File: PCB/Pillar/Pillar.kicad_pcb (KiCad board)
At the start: 2 copper layers, 100 x 86.6 mm, 39 parts, among them CN1 GROVE, CN2 GROVE, CN3 GROVE, CN4 GROVE, CN5 GROVE, CN6 TTL-232R-3V3, CN7 ST-LINK, CN8 Conn_01x05_Female, CN9 CardEdgeConnector5P, SW1 RESET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

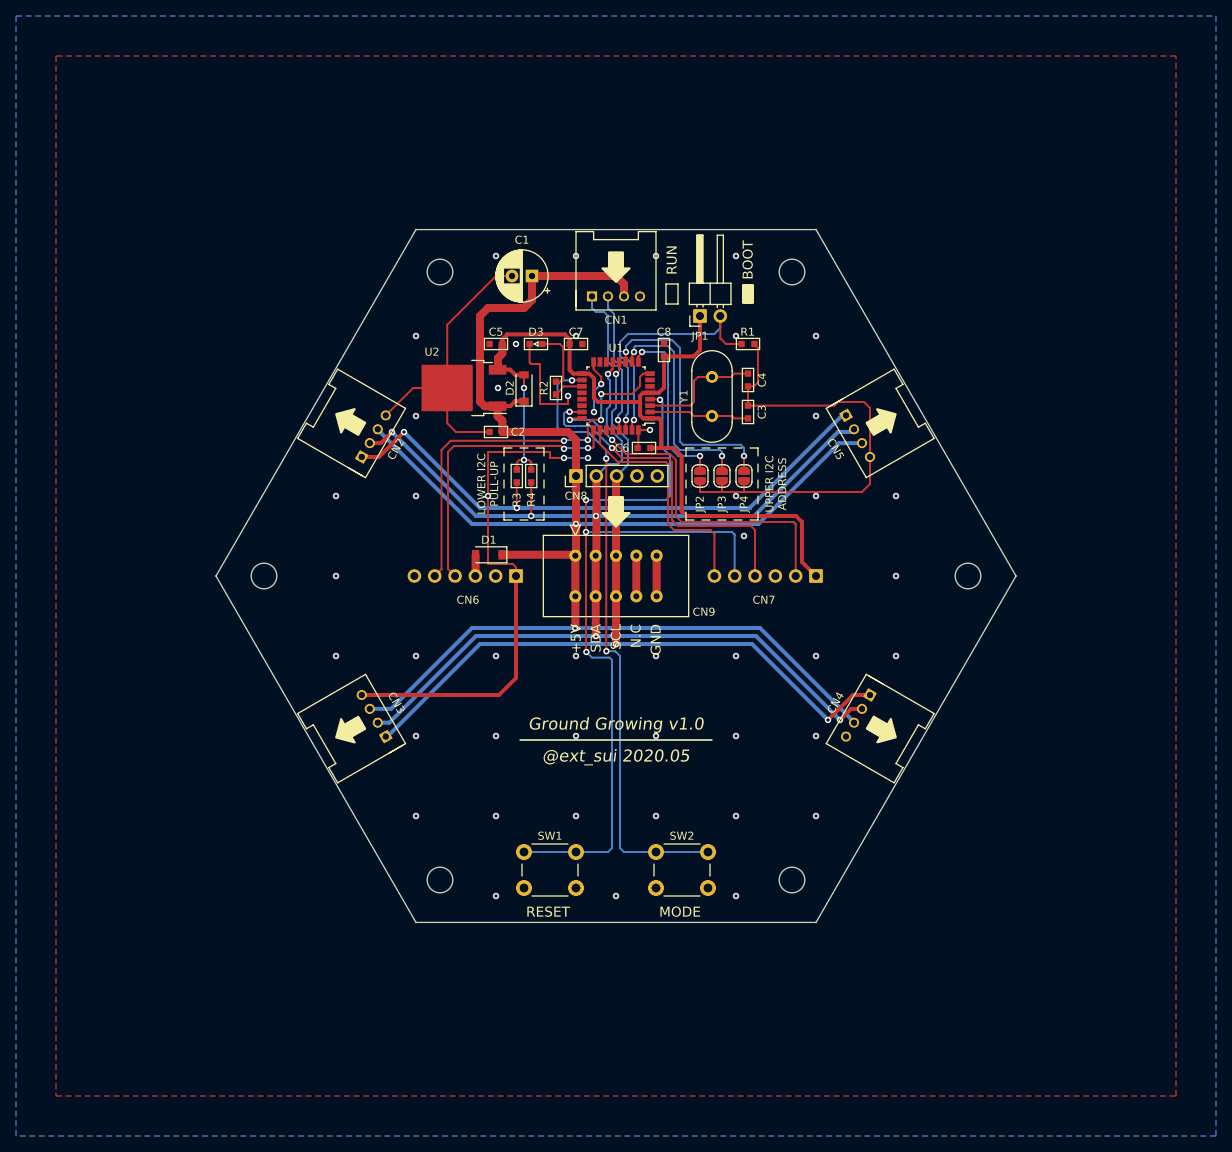
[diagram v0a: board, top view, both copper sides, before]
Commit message: (Pcb) ネットリストを修正してフットプリント配置エラーを解決 #60
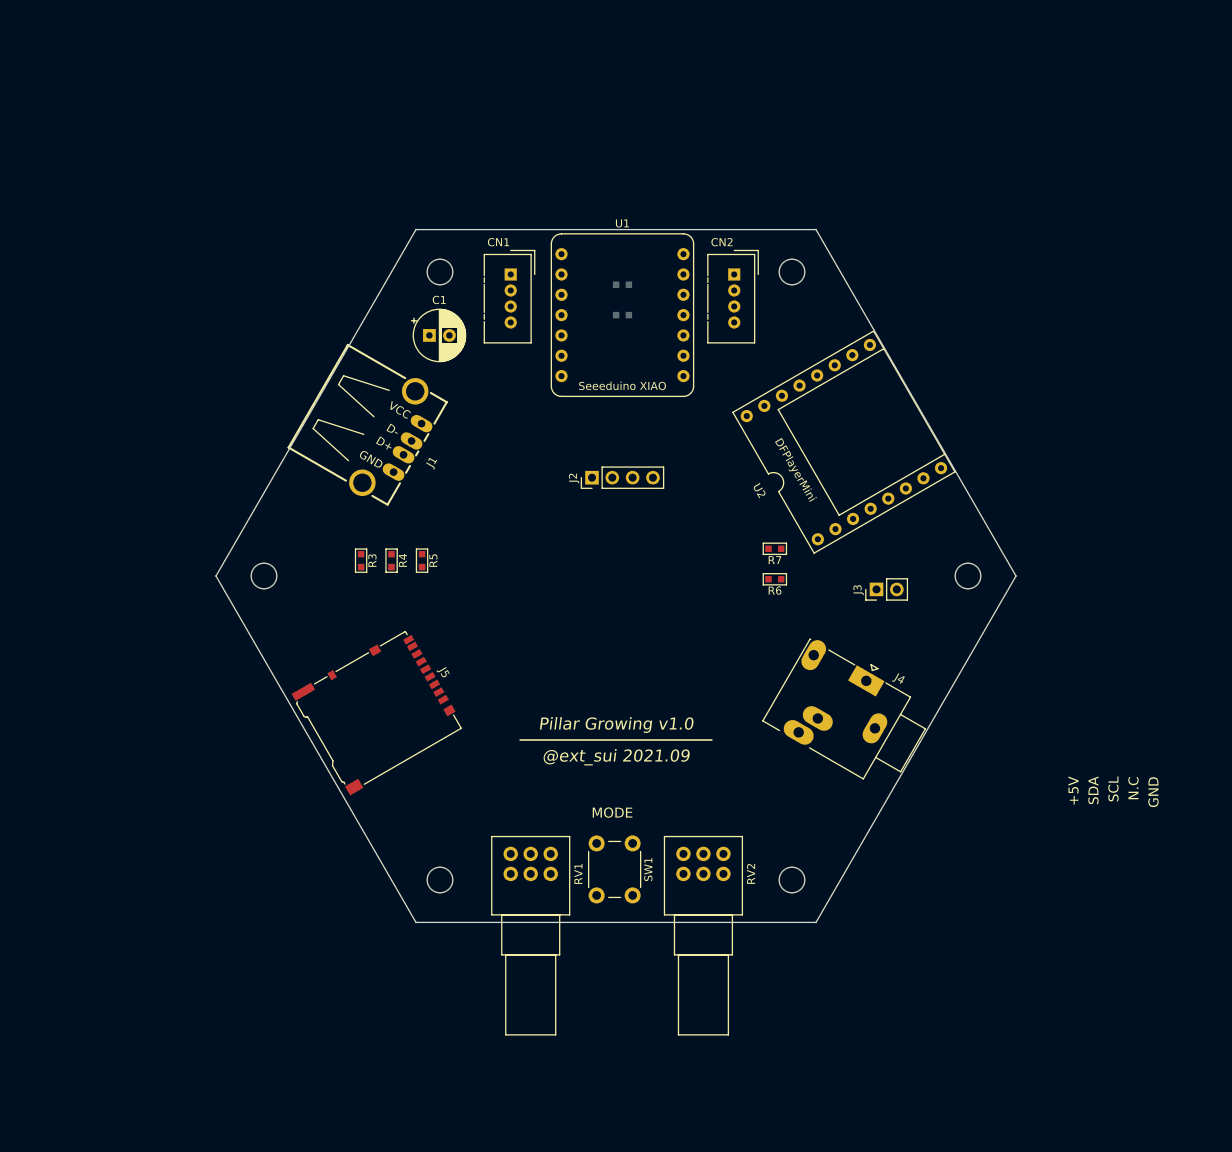
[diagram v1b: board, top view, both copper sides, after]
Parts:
- removed C2: 0.1uF, extsui:C_1608_HandSolderingCustom
- removed C3, C4: 22pF, extsui:C_1608_HandSolderingCustom
- removed C5: 10uF, extsui:C_1608_HandSolderingCustom
- removed C6, C7, C8: 0.1u, extsui:C_1608_HandSolderingCustom
- removed CN3, CN4, CN5: GROVE, OPL_Connector:HW4-2.0-90D
- removed CN6: TTL-232R-3V3, Connector_PinHeader_2.54mm:PinHeader_1x06_P2.54mm_Horizontal
- removed CN7: ST-LINK, Connector_PinHeader_2.54mm:PinHeader_1x06_P2.54mm_Horizontal
- removed CN8: Conn_01x05_Female, Connector_PinHeader_2.54mm:PinHeader_1x05_P2.54mm_Vertical
- removed CN9: CardEdgeConnector5P, extsui:CONN_CARD_EDGE_395-010-521-201
- removed D1, D2: SS2040FL, Diode_SMD:D_SOD-123
- removed D3: LED, extsui:LED_1608_HandSolderingCustom
- removed JP1: JP_BOOT, Connector_PinHeader_2.54mm:PinHeader_1x02_P2.54mm_Horizontal
- removed JP2, JP3, JP4: Jumper_NO_Small, Jumper:SolderJumper-2_P1.3mm_Open_RoundedPad1.0x1.5mm
- removed SW2: MODE, Button_Switch_THT:SW_PUSH_6mm_H8mm
- removed Y1: 8MHz, Crystal:Crystal_HC49-4H_Vertical
- added J1: USB_A, OPL_Connector:USB4+2P-2.0-90D, F.Cu at (101.6, 87.6)
- added J2: OLED_128x64_IIC, Connector_PinHeader_2.54mm:PinHeader_1x04_P2.54mm_Vertical, F.Cu at (127.0, 92.7)
- added J3: Speaker, Connector_PinHeader_2.54mm:PinHeader_1x02_P2.54mm_Vertical, F.Cu at (162.6, 106.7)
- added J4: AudioJack3_SwitchTR, Connector_Audio:Jack_3.5mm_Ledino_KB3SPRS_Horizontal, F.Cu at (161.3, 118.1)
- added J5: Micro_SD_Card_Det_Hirose_DM3AT, Connector_Card:microSD_HC_Hirose_DM3AT-SF-PEJM5, F.Cu at (100.3, 121.9)
- added R5: 4.7k, extsui:C_1608_HandSolderingCustom, F.Cu at (105.8, 103.1)
- added R6: 1k, extsui:C_1608_HandSolderingCustom, F.Cu at (149.9, 105.4)
- added R7: 1k, extsui:C_1608_HandSolderingCustom, F.Cu at (149.9, 101.6)
- added RV1: BRIGHTNESS, Potentiometer_THT:Potentiometer_Alps_RK097_Dual_Horizontal, F.Cu at (116.8, 142.2)
- added RV2: MP3_VOLUME, Potentiometer_THT:Potentiometer_Alps_RK097_Dual_Horizontal, F.Cu at (138.4, 142.2)
- C1: value 47uF -> 100u
- CN1, CN2: value GROVE -> GROVE_IIC_5V; footprint OPL_Connector:HW4-2.0-90D -> Connector:NS-Tech_Grove_1x04_P2mm_Vertical
- R1, R2: value 10k -> 4.7k; moved to B.Cu
- R3, R4: value 10k -> 4.7k
- SW1: value RESET -> MDOE; footprint Button_Switch_THT:SW_PUSH_6mm_H8mm -> Button_Switch_THT:SW_PUSH_6mm_H8.5mm
- U1: value STM32F303K8T6 -> SeeeduinoXIAO; footprint Package_QFP:LQFP-32_7x7mm_P0.8mm -> extsui:SeeeduinoXIAO
- U2: value NJM2845DL1-33 -> DFPlayerMini; footprint Package_TO_SOT_SMD:TO-252-2 -> extsui:DFPlayerMini
- moved CN2 51.3 mm to (144.8, 67.3), turned to 0 degrees
- moved U2 39.6 mm to (148.6, 94.0), turned to 120 degrees
- moved R3 22.2 mm to (98.1, 103.1)
- moved R4 20.4 mm to (101.9, 103.1)
- moved U1 20.3 mm to (130.8, 62.2), turned to 0 degrees
- moved R1 17.4 mm to (130.8, 68.6), turned to 180 degrees
- moved C1 14.8 mm to (106.7, 74.9), turned to 0 degrees
- moved CN1 13.2 mm to (116.8, 67.3)
- moved R2 12.3 mm to (130.8, 72.4), turned to 180 degrees
- moved SW1 9.01 mm to (132.1, 138.4), turned to 270 degrees
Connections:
- CN1 pad 1: UPPER_SCL -> SCL
- CN1 pad 2: UPPER_SDA -> SDA
- CN2 pad 1: LOWER_SCL -> SCL
- CN2 pad 2: LOWER_SDA -> SDA
- R1 pad 1: Net-(JP1-Pad2) -> 3V3
- R1 pad 2: GND -> SDA
- R2 pad 1: Net-(R2-Pad1) -> 3V3
- R2 pad 2: Net-(D3-Pad2) -> SCL
- R3 pad 2: LOWER_SCL -> CS
- R4 pad 2: LOWER_SDA -> MOSI
- SW1 pad 1: GND -> Net-(SW1-Pad1)
- SW1 pad 2: NRST -> GND
- U1 pad 1: 3V3 -> RV_B
- U1 pad 10: Net-(JP3-Pad2) -> MISO
- U1 pad 11: Net-(JP4-Pad2) -> MOSI
- U1 pad 12: LOWER_SCL -> 3V3
- U1 pad 13: LOWER_SDA -> GND
- U1 pad 14: Net-(U1-Pad14) -> 5V
- U1 pad 2: Net-(C3-Pad1) -> RV_V
- U1 pad 3: Net-(C4-Pad1) -> CS
- U1 pad 4: NRST -> Net-(SW1-Pad1)
- U1 pad 5: 3V3 -> SDA
- U1 pad 6: Net-(U1-Pad6) -> SCL
- U1 pad 7: Net-(U1-Pad7) -> TXD
- U1 pad 9: Net-(JP2-Pad2) -> SCK
- U2 pad 2: GND -> Net-(R6-Pad1)
- U2 pad 3: 3V3 -> Net-(R7-Pad1)
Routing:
- net 5V: track 226.3 -> 0.00 mm, vias 2 -> 0
- net GND: track 192.9 -> 0.00 mm, vias 50 -> 0
- net LOWER_SCL: track 182.8 -> 0.00 mm, vias 6 -> 0
- net LOWER_SDA: track 182.5 -> 0.00 mm, vias 6 -> 0
- net 3V3: track 106.3 -> 0.00 mm, vias 2 -> 0
- net NRST: track 105.9 -> 0.00 mm, vias 4 -> 0
- net Net-(SW2-Pad1): track 79.4 -> 0.00 mm, vias 3 -> 0
- net RXD: track 49.9 -> 0.00 mm, vias 4 -> 0
- net SWCLK: track 45.9 -> 0.00 mm, vias 2 -> 0
- net SWDIO: track 43.0 -> 0.00 mm, vias 2 -> 0
- net TXD: track 36.7 -> 0.00 mm, vias 2 -> 0
- net Net-(JP1-Pad2): track 32.6 -> 0.00 mm, vias 1 -> 0
- net Net-(JP4-Pad2): track 32.3 -> 0.00 mm, vias 2 -> 0
- net SWO: track 30.4 -> 0.00 mm
- net Net-(JP3-Pad2): track 27.6 -> 0.00 mm, vias 2 -> 0
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- removed copper zone on B.Cu, net GND
- removed copper zone on F.Cu, net GND
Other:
- board text added: "@ext_sui 2021.09"
- board text added: "Pillar Growing v1.0"
- board text removed: "3V3"
- board text removed: "5"
- board text removed: "@ext_sui 2020.05"
- board text removed: "BOOT"
- board text removed: "CTS"
- board text removed: "D"
- board text removed: "G"
- board text removed: "Ground Growing v1.0"
- board text removed: "LOWER I2C PULL-UP"
- board text removed: "NRST"
- board text removed: "RESET"
- board text removed: "RTS"
- board text removed: "RUN"
- board text removed: "RXD"
- board text removed: "S"
- board text removed: "ST-LINK"
- board text removed: "SWCLK"
- board text removed: "SWDIO"
- board text removed: "SWO"
- board text removed: "TTL-232R-3V3"
- board text removed: "TXD"
- board text removed: "UPPER I2C ADDRESS"
- board text removed: "×"

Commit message: (Pcb) OLED のフットプリント追加と各種パーツの位置修正 #60
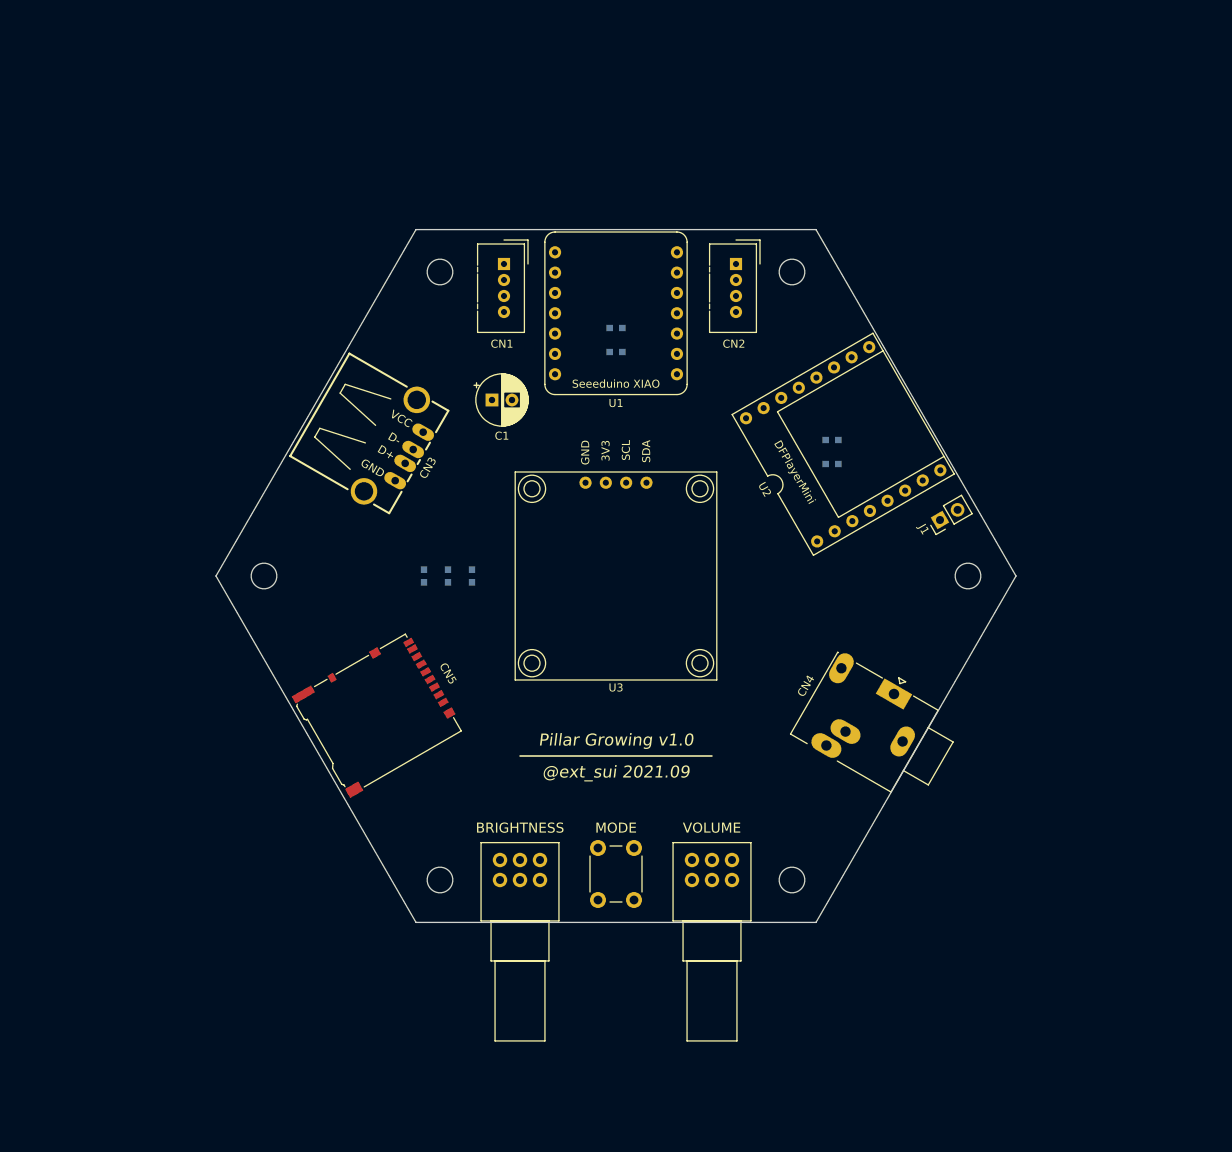
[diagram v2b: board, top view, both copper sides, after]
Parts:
- removed J2: OLED_128x64_IIC, Connector_PinHeader_2.54mm:PinHeader_1x04_P2.54mm_Vertical
- removed J3: Speaker, Connector_PinHeader_2.54mm:PinHeader_1x02_P2.54mm_Vertical
- removed J4: AudioJack3_SwitchTR, Connector_Audio:Jack_3.5mm_Ledino_KB3SPRS_Horizontal
- removed J5: Micro_SD_Card_Det_Hirose_DM3AT, Connector_Card:microSD_HC_Hirose_DM3AT-SF-PEJM5
- added CN3: USB_A, OPL_Connector:USB4+2P-2.0-90D, F.Cu at (101.8, 88.7)
- added CN4: AudioJack3_SwitchTR, Connector_Audio:Jack_3.5mm_Ledino_KB3SPRS_Horizontal, F.Cu at (164.8, 119.8)
- added CN5: Micro_SD_Card_Det_Hirose_DM3AT, Connector_Card:microSD_HC_Hirose_DM3AT-SF-PEJM5, F.Cu at (100.3, 122.2)
- added U3: OLED_128x64_IIC, extsui:OLED_128x64_0.96inch, F.Cu at (130.0, 92.0)
- J1: value USB_A -> Speaker; footprint OPL_Connector:USB4+2P-2.0-90D -> Connector_PinHeader_2.54mm:PinHeader_1x02_P2.54mm_Vertical
- R3, R4, R5, R6, R7: moved to B.Cu
- RV2: value MP3_VOLUME -> VOLUME
- moved J1 69.7 mm to (170.5, 98.0), turned to 120 degrees
- moved R6 16.1 mm to (157.0, 91.0)
- moved R7 15.4 mm to (157.0, 88.0)
- moved R3 14.0 mm to (112.0, 105.0), turned to 90 degrees
- moved C1 11.2 mm to (114.5, 83.0)
- moved R4 7.31 mm to (109.0, 105.0), turned to 90 degrees
- moved R1 5.48 mm to (130.0, 74.0)
- moved R2 4.68 mm to (130.0, 77.0)
- moved R5 1.93 mm to (106.0, 105.0), turned to 90 degrees
- moved CN1 1.56 mm to (116.0, 66.0)
- moved RV1 1.54 mm to (115.5, 143.0)
- moved CN2 1.33 mm to (145.0, 66.0)
- moved RV2 1.31 mm to (139.5, 143.0)
- moved U1 0.84 mm to (130.0, 62.0)
- moved SW1 0.59 mm to (132.2, 139.0)
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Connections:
- J1 pad 1: 5V -> Net-(J1-Pad1)
- RV1 pad 1: GND -> Net-(RV1-Pad1)
- RV1 pad 2: RV_B -> Net-(RV1-Pad2)
- RV1 pad 3: 3V3 -> Net-(RV1-Pad3)
- RV1 pad 4: Net-(RV1-Pad4) -> GND
- RV1 pad 5: Net-(RV1-Pad5) -> RV_B
- RV1 pad 6: Net-(RV1-Pad6) -> 3V3
- RV2 pad 1: GND -> Net-(RV2-Pad1)
- RV2 pad 2: RV_V -> Net-(RV2-Pad2)
- RV2 pad 3: 3V3 -> Net-(RV2-Pad3)
- RV2 pad 4: Net-(RV2-Pad4) -> GND
- RV2 pad 5: Net-(RV2-Pad5) -> RV_V
- RV2 pad 6: Net-(RV2-Pad6) -> 3V3
- U2 pad 6: Net-(J3-Pad1) -> Net-(J1-Pad1)
- U2 pad 8: Net-(J3-Pad2) -> Net-(J1-Pad2)
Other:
- board text added: "3V3"
- board text added: "BRIGHTNESS"
- board text added: "VOLUME"
- board text removed: "+5V"
- board text removed: "N.C"

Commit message: (Pcb) Mode スイッチの割り当て変更と抵抗のディスクリート部品化 #60
* Mode スイッチの割り当ては XIAO 拡張ボードの UserButton に合わせたため。
* ディスクリート化は基板領域が余っているため。
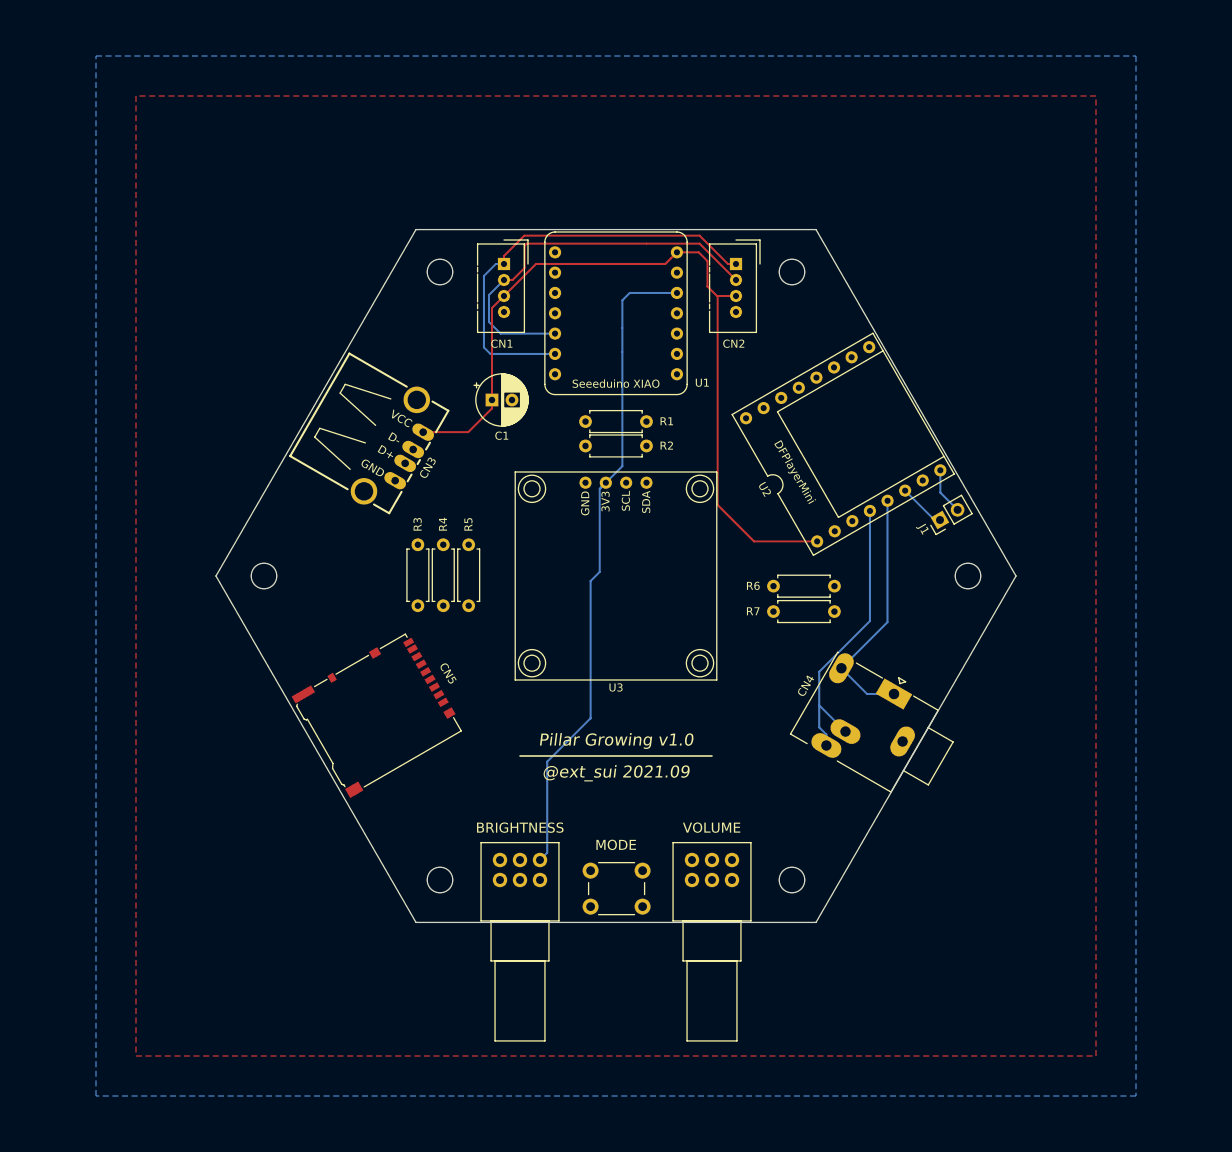
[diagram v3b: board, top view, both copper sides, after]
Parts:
- R1, R2, R3, R4, R5, R6, R7: footprint extsui:C_1608_HandSolderingCustom -> Resistor_THT:R_Axial_DIN0207_L6.3mm_D2.5mm_P7.62mm_Horizontal; moved to F.Cu
- moved R7 22.7 mm to (149.7, 109.4), turned to 0 degrees
- moved R6 16.9 mm to (149.7, 106.3), turned to 0 degrees
- moved R2 12.3 mm to (133.8, 88.7)
- moved R1 12.3 mm to (133.8, 85.7)
- moved R3 7.81 mm to (105.2, 101.1), turned to 270 degrees
- moved R5 6.82 mm to (111.6, 101.1), turned to 270 degrees
- moved SW1 6.12 mm to (126.8, 141.8), turned to 0 degrees
- moved R4 3.95 mm to (108.4, 101.1), turned to 270 degrees
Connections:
- U1 pad 1: RV_B -> RV_V
- U1 pad 2: RV_V -> Net-(SW1-Pad1)
- U1 pad 4: Net-(SW1-Pad1) -> RV_B
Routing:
- net 5V: track 0.00 -> 100.3 mm
- net 3V3: track 0.00 -> 82.4 mm
- net SCL: track 0.00 -> 53.8 mm
- net SDA: track 0.00 -> 49.3 mm
- net Net-(CN4-PadR): track 0.00 -> 37.0 mm
- net Net-(CN4-PadT): track 0.00 -> 31.2 mm
- net Net-(J1-Pad1): track 0.00 -> 5.88 mm
- net Net-(J1-Pad2): track 0.00 -> 5.83 mm
- added copper zone on B.Cu, net GND
- added copper zone on F.Cu, net GND
